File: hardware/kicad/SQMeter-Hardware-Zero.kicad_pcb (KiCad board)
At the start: 2 copper layers, 125 x 82 mm, 46 parts, among them J1 12V IN, J10 AUX, J11 Zero left, J12 Zero right, J3 I2C TSL2591, J4 I2C MLX90614, J5 I2C BME280, J6 I2C SPARE, J7 GPS, J8 RG-15, J9 WIND, Q1 AO3401A, U1 AP63205WU, U4 USBLC6-2SC6, U5 USBLC6-2SC6, U6 USBLC6-2SC6

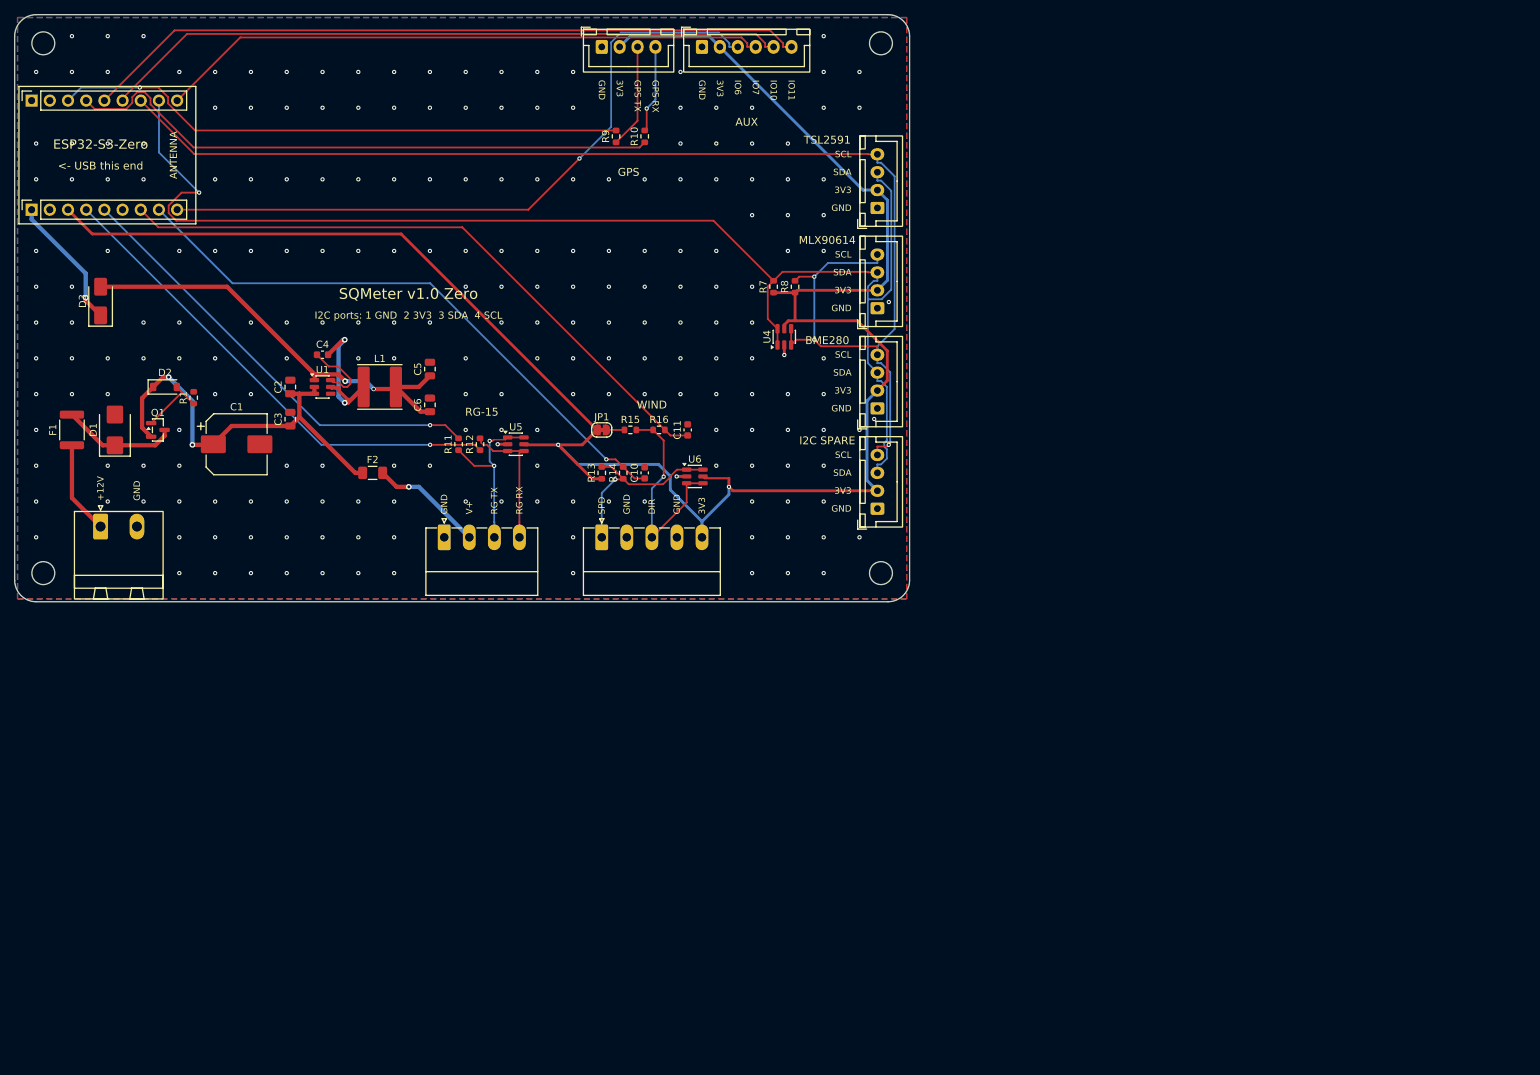
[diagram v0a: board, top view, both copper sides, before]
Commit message: fix: centre boards on the A4 sheet instead of hanging off the page origin
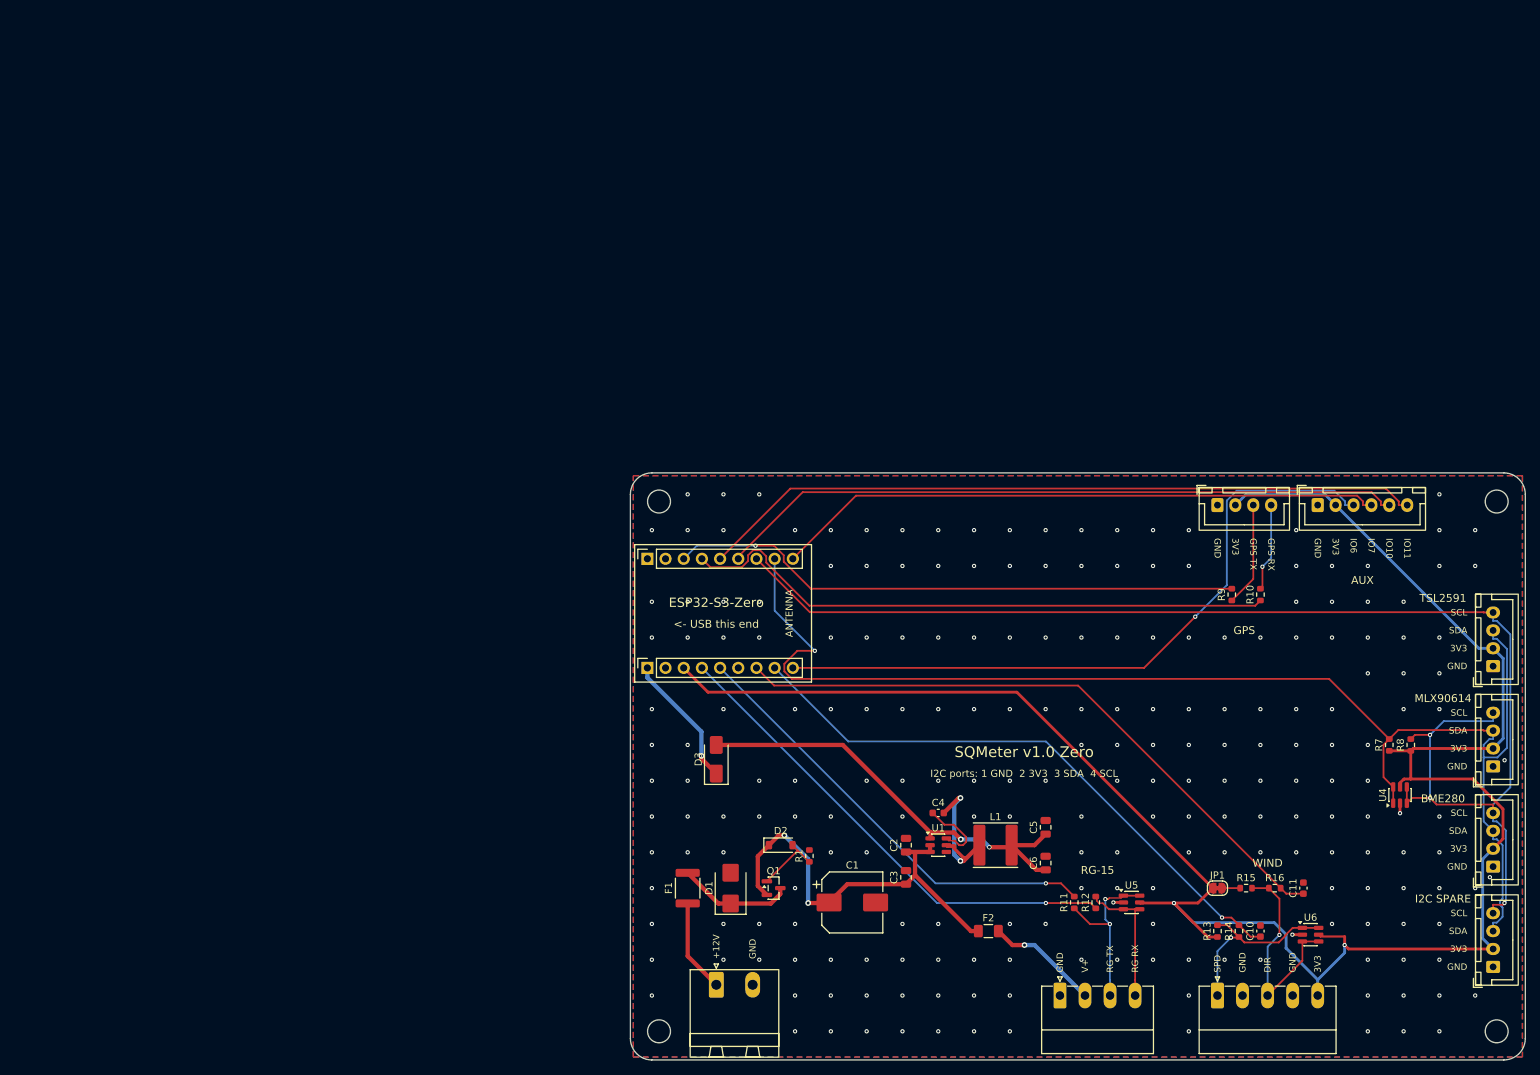
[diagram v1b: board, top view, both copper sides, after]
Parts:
- moved C1 107.2 mm to (117.0, 124.0)
- moved C10 107.2 mm to (174.0, 128.0)
- moved C11 107.2 mm to (180.0, 122.0)
- moved C2 107.2 mm to (124.5, 116.0)
- moved C3 107.2 mm to (124.5, 120.5)
- moved C4 107.2 mm to (129.0, 111.5)
- moved C5 107.2 mm to (144.0, 113.5)
- moved C6 107.2 mm to (144.0, 118.5)
- moved D1 107.2 mm to (100.0, 122.0)
- moved D2 107.2 mm to (107.0, 116.0)
- moved D3 107.2 mm to (98.0, 104.0)
- moved F1 107.2 mm to (94.0, 122.0)
- moved F2 107.2 mm to (136.0, 128.0)
- moved H1 107.2 mm to (90.0, 68.0)
- moved H2 107.2 mm to (207.0, 68.0)
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
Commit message: feat: second I2C bus for a second TSL2591 (SQM + SQM-L)
TSL2591 has a fixed address, so the second sensor gets its own bus on
GPIO10/11 (I2C-2 JST-XH port, own pull-ups and ESD). AUX drops to IO6/IO7.
Q1 gate zener replaced by a resistor divider (one fewer extended part).
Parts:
- removed D2: BZT52C10, Diode_SMD:D_SOD-123
- added J13: I2C-2 TSL2591 #2, Connector_JST:JST_XH_B4B-XH-A_1x04_P2.50mm_Vertical, F.Cu at (195.0, 68.5)
- added R19: 10k, Resistor_SMD:R_0603_1608Metric, F.Cu at (107.0, 115.0)
- added R20: 4.7k, Resistor_SMD:R_0603_1608Metric, F.Cu at (185.0, 82.5)
- added R21: 4.7k, Resistor_SMD:R_0603_1608Metric, F.Cu at (188.0, 82.5)
- added U7: USBLC6-2SC6, Package_TO_SOT_SMD:SOT-23-6, F.Cu at (192.0, 85.0)
- J10: footprint Connector_JST:JST_XH_B6B-XH-A_1x06_P2.50mm_Vertical -> Connector_JST:JST_XH_B4B-XH-A_1x04_P2.50mm_Vertical
- J3: value I2C TSL2591 -> I2C TSL2591 #1
- moved H2 7.52 mm to (207.5, 75.5)
- moved J10 0.50 mm to (181.5, 68.5)
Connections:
- J12 pad 5: /AUX4 -> /SCL2
- J12 pad 6: /AUX3 -> /SDA2
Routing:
- net /SCL2: track 0.00 -> 127.8 mm, vias 0 -> 1
- net /SDA2: track 0.00 -> 118.4 mm, vias 0 -> 1
- net /AUX4: track 101.3 -> 0.00 mm
- net /AUX3: track 96.0 -> 0.00 mm
- net +3V3: track 283.4 -> 309.1 mm, vias 2 -> 6
- net /SDA: track 187.3 -> 200.7 mm
- net /SCL: track 191.6 -> 178.1 mm, vias 3 -> 2
- net /SW: track 20.2 -> 11.6 mm, vias 2 -> 0
- net /Q1_G: track 9.42 -> 17.0 mm, vias 0 -> 2
- net /AUX1: track 96.6 -> 89.2 mm, vias 1 -> 0
- net /WDIR_EXT: track 30.5 -> 24.5 mm
- net +5V: track 59.7 -> 65.7 mm, vias 2 -> 3
- net +12V: track 57.8 -> 62.0 mm
- net /BST: track 10.1 -> 13.1 mm, vias 0 -> 2
- net /RG_RXI: track 19.2 -> 20.7 mm, vias 0 -> 1
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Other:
- board text added: "I2C-2"
- board text added: "TSL2591 #1"
- board text removed: "IO10"
- board text removed: "IO11"
- board text removed: "TSL2591"

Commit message: feat: brand lockup on silkscreen, hardware Rev A, JLC-ready gerber zips
- SQMeter lockup (brand kit silkscreen mark + Inter SemiBold name) as plain
  silkscreen polygons from brand_silk.json; no font install needed
- HW_REV = A: on the silkscreen, KiCad title blocks, gerber metadata and fab
  file names; versioned separately from firmware
- drop the verbose I2C pinout line; per-pin labels already cover it
- gerber zip holds only fab layers + drill files
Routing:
- net /SDA2: track 118.4 -> 148.9 mm, vias 1 -> 3
- net /SDA: track 200.7 -> 177.7 mm, vias 1 -> 2
- net /SCL2: track 127.8 -> 120.1 mm, vias 1 -> 0
- net +3V3: track 309.1 -> 316.8 mm, vias 6 -> 3
- net /WIND_SPD: track 83.4 -> 88.0 mm, vias 1 -> 0
- net /RG_RXI: track 20.7 -> 25.1 mm, vias 1 -> 2
- net +12V: track 62.0 -> 64.8 mm
- net /Q1_G: track 17.0 -> 19.6 mm
- net /GPS_TX: track 83.0 -> 81.1 mm, vias 3 -> 0
- net /RG_TX: track 68.9 -> 70.7 mm
- net /AUX1: track 89.2 -> 87.5 mm, vias 0 -> 1
- net /AUX2: track 84.8 -> 83.7 mm
- net /RG_TXO: track 24.7 -> 23.6 mm, vias 2 -> 1
- net /WIND_DIR: track 89.5 -> 90.5 mm
- net /BST: track 13.1 -> 12.3 mm
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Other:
- board text added: "Rev A S3-Zero"
- board text removed: "I2C ports: 1 GND 2 3V3 3 SDA 4 SCL"
- board text removed: "SQMeter v1.0 Zero"

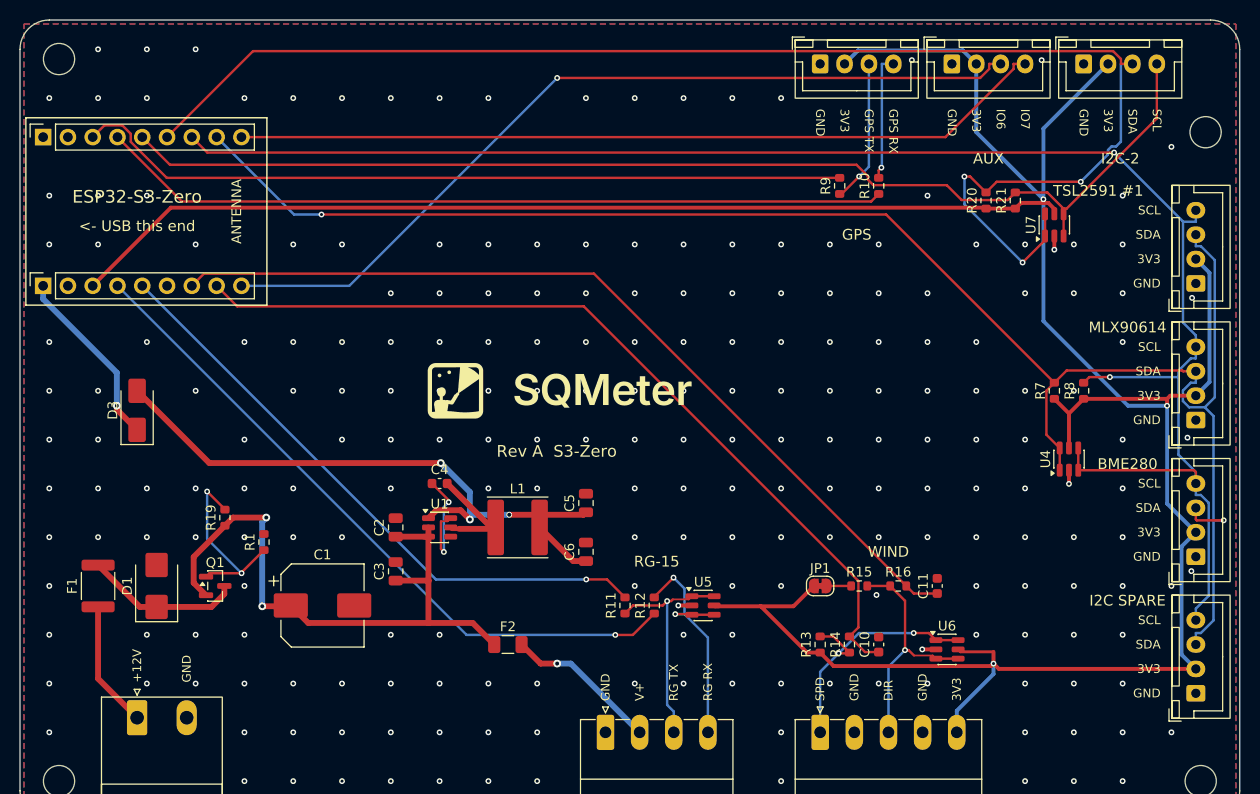
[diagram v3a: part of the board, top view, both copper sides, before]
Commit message: feat: Inter Bold silkscreen (embedded), black mask / white silk stackup
- all silkscreen text and references in Inter Bold, min 1.2 mm; font embedded in
  the board files so they open the same without Inter installed
- stroke widths measured on plotted gerbers (>0.15 mm); KiCad's TrueType
  thickness check ignored as it flags every size of the variable font
- stackup: black solder mask, white silkscreen (3D view; colour is picked at order)
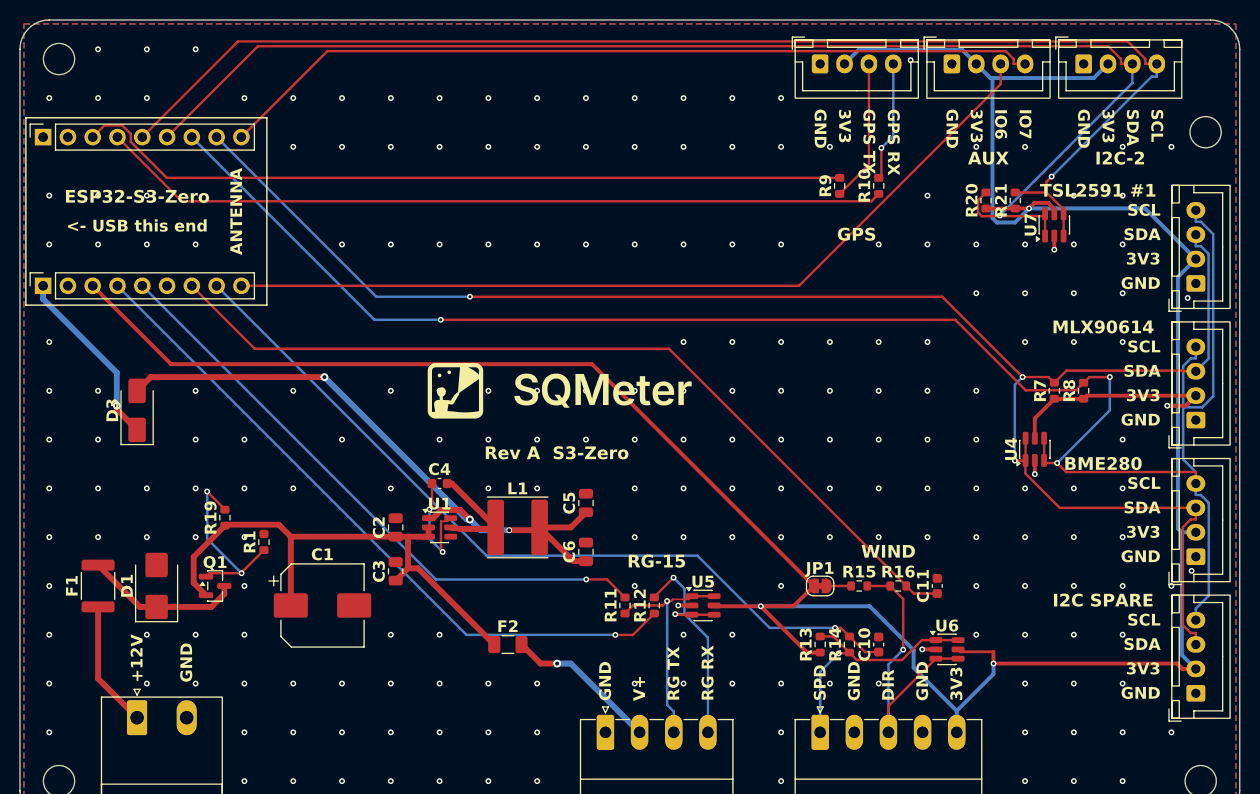
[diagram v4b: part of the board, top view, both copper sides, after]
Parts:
- moved U4 3.64 mm to (190.0, 108.0)
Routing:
- net /SCL2: track 120.1 -> 135.8 mm, vias 0 -> 1
- net /SCL: track 177.8 -> 190.4 mm, vias 2 -> 3
- net /SDA2: track 148.9 -> 136.8 mm, vias 3 -> 1
- net +12V: track 64.8 -> 55.5 mm, vias 2 -> 0
- net +3V3: track 316.8 -> 310.3 mm, vias 3 -> 4
- net /WDIR_EXT: track 24.5 -> 30.4 mm
- net /WIND_SPD: track 88.0 -> 83.4 mm, vias 0 -> 1
- net /SDA: track 177.7 -> 174.9 mm, vias 2 -> 3
- net /WSPD_EXT: track 27.1 -> 26.0 mm, vias 2 -> 1
- net /AUX2: track 83.7 -> 84.8 mm
- net /WIND_DIR: track 90.5 -> 89.5 mm
- net /AUX1: track 87.5 -> 88.4 mm, vias 1 -> 0
- net /GPS_RXI: track 13.0 -> 12.3 mm
- net +5V: track 65.7 -> 65.0 mm
- net /GPS_TXO: track 14.7 -> 14.6 mm, vias 1 -> 0
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
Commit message: feat: ESP32-S3-ETH PoE home board and Li-ion travel board
- eth: Waveshare ESP32-S3-ETH (+ PoE module) on 2x20 sockets, PoE or 12 V in,
  MT3608 boost keeps the RG-15 at 12.6 V on PoE; own GPIO map (W5500 owns 9-14)
- travel: ESP32-S3-Zero, USB-C only, MCP73871 power-path Li-ion charger with
  NTC cold-charge cut-off, power slide switch, battery/charger status on GPIO,
  OLED port; 85 x 66 mm, no field wiring
- connector titles placed relative to their connector so layouts can differ
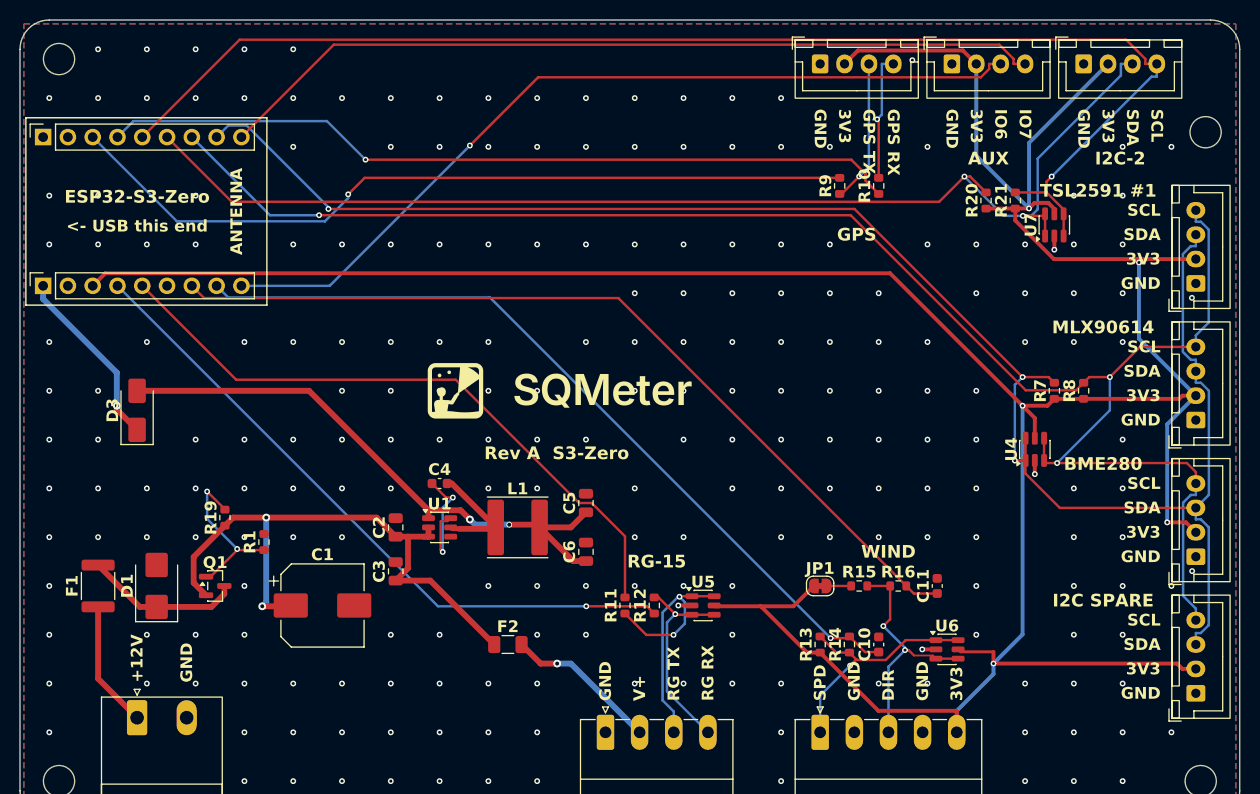
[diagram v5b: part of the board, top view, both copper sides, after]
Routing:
- net +3V3: track 310.3 -> 336.7 mm, vias 4 -> 5
- net /SDA2: track 136.8 -> 122.1 mm, vias 1 -> 2
- net /SCL: track 190.4 -> 176.8 mm
- net +12V: track 55.5 -> 62.0 mm, vias 0 -> 2
- net /RG_TXO: track 23.6 -> 29.2 mm, vias 1 -> 2
- net +5V: track 65.0 -> 59.4 mm, vias 3 -> 2
- net /WDIR_EXT: track 30.4 -> 25.1 mm, vias 1 -> 2
- net /RG_RXI: track 25.1 -> 21.1 mm, vias 2 -> 1
- net /RG_RX: track 62.7 -> 66.4 mm, vias 1 -> 0
- net /Q1_G: track 19.6 -> 17.0 mm
- net /GPS_RX: track 79.8 -> 82.2 mm, vias 0 -> 1
- net /RG_TX: track 70.7 -> 68.9 mm
- net /SDA: track 174.9 -> 176.7 mm
- net /GPS_TX: track 81.0 -> 82.2 mm, vias 0 -> 1
- net /BST: track 12.0 -> 13.1 mm
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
